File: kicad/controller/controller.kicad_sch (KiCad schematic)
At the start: 39 parts, among them J1 Conn_02x04_Top_Bottom, SW0 1825910-6, SW2 1825910-6, SW3 SW_SPST, SW4 1825910-6, SW6 1825910-6, U1 MCP23S08T-E/SO, U2 MCP3008

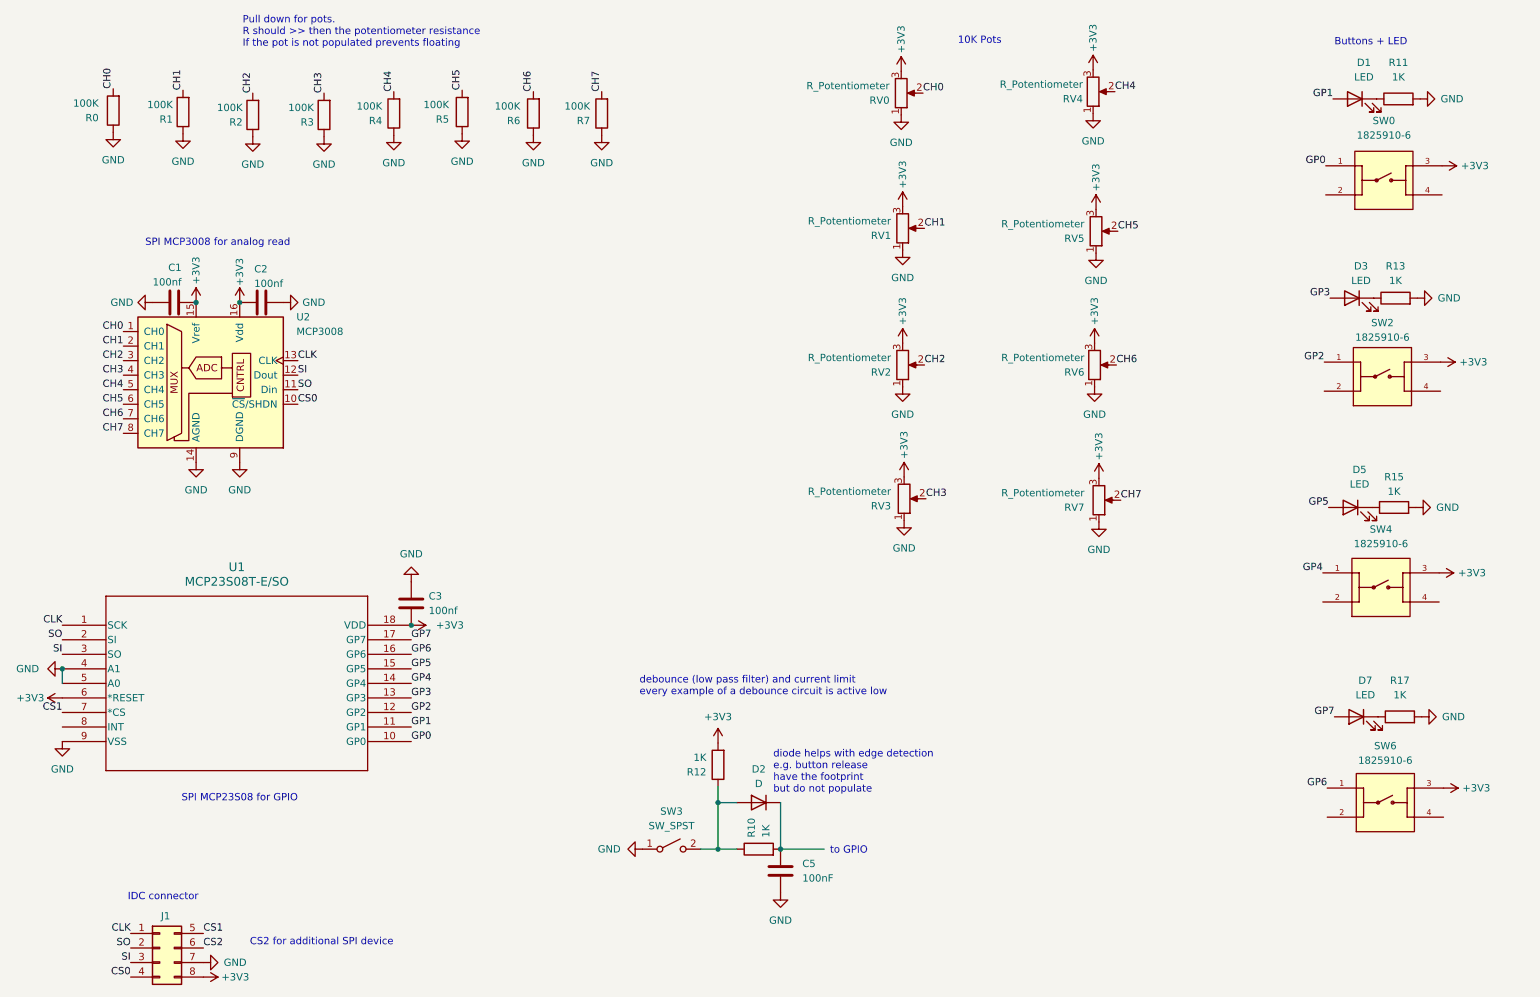
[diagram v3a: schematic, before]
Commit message: fix button behaviour now I have a PCB
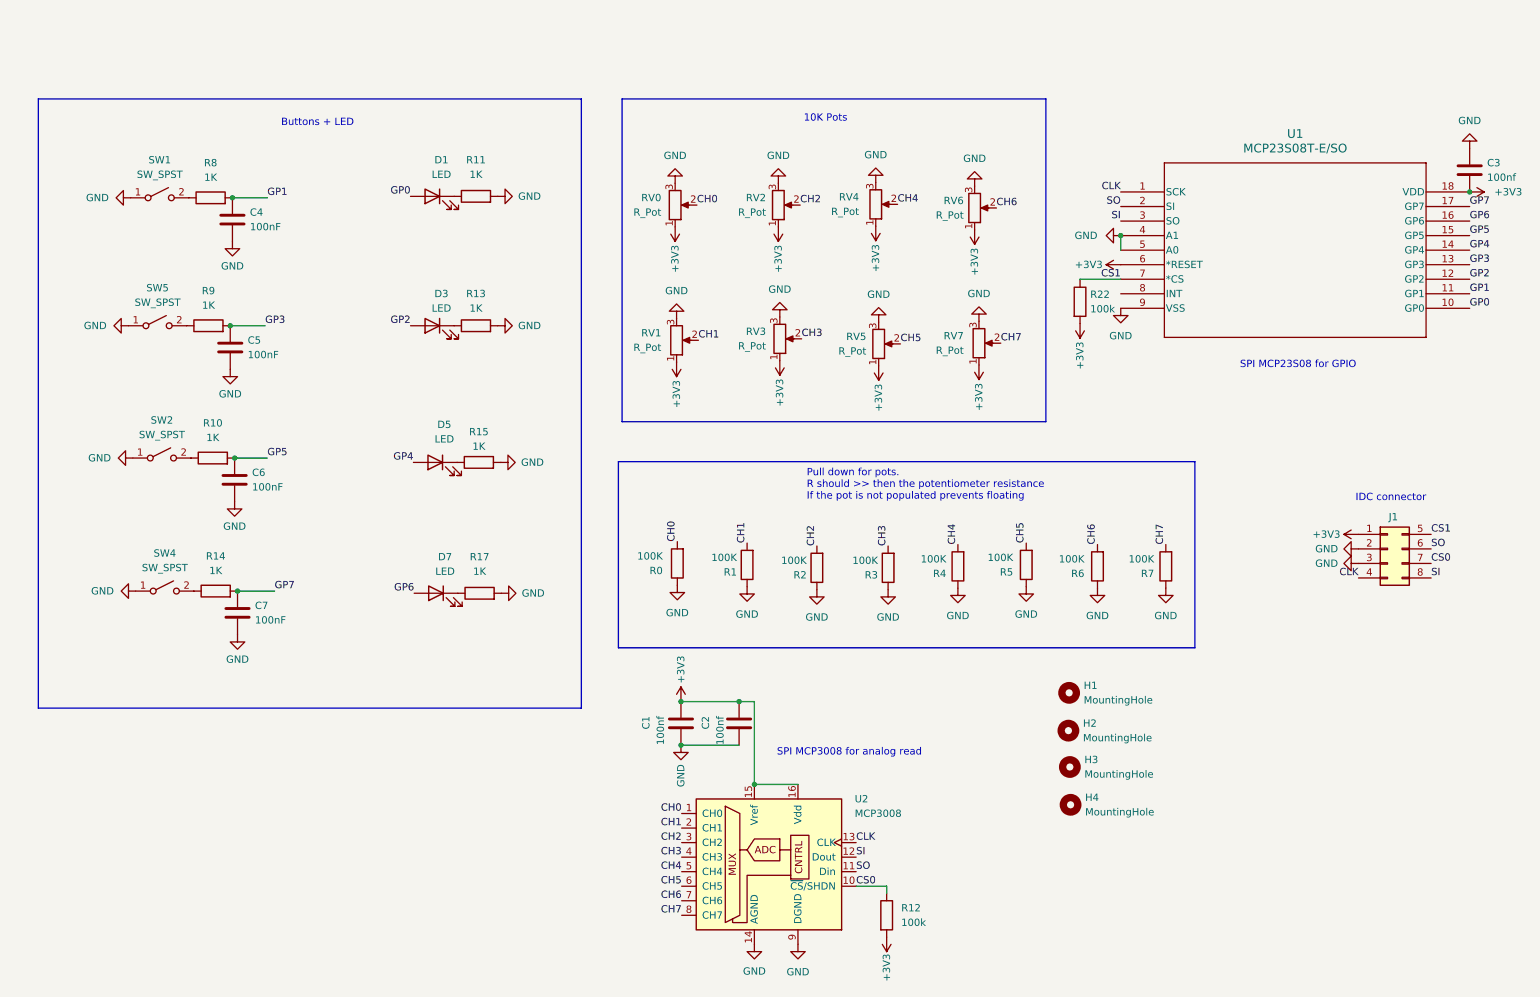
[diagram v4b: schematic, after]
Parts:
- removed D2: D, symbol Device:D
- removed SW0, SW2, SW4, SW6: 1825910-6, Library:SW_1825910-6-4, symbol 2024-07-07_06-52-22:1825910-6
- removed SW3: SW_SPST, symbol Switch:SW_SPST
- added C4, C6, C7: 100nF, symbol Device:C
- added H1, H2, H3, H4: MountingHole, MountingHole:MountingHole_2.7mm_M2.5, symbol Mechanical:MountingHole
- added R14, R8, R9: 1K, symbol Device:R
- added R22: 100k, Resistor_SMD:R_0805_2012Metric, symbol Device:R
- added SW1, SW2, SW4, SW5: SW_SPST, Button_Switch_THT:SW_PUSH-12mm, symbol Switch:SW_SPST
- R12: value 1K -> 100k; footprint (none) -> Resistor_SMD:R_0805_2012Metric
- RV0, RV1, RV2, RV3, RV4, RV5, RV6, RV7: value R_Potentiometer -> R_Pot; footprint Potentiometer_THT:Potentiometer_Alps_RK09K_Single_Vertical -> Potentiometer_THT:Potentiometer_Bourns_PTV09A-1_Single_Vertical
- U1: footprint Library:SOIC18-W_MC_MCH -> Custom:SOIC18-W_MC_MCH
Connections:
- net CS2 is gone; now on net SO: J1.6 (Pin_6)
- net +3V3: now also J1.1 (Pin_1), RV0.1, RV1.1, RV2.1, RV3.1, RV4.1, RV5.1, RV6.1, RV7.1, R22.2; no longer J1.8 (Pin_8), RV0.3, RV1.3, RV2.3, RV3.3, RV4.3, RV5.3, RV6.3, RV7.3
- net CLK: now also J1.4 (Pin_4); no longer J1.1 (Pin_1)
- net CS0: now also J1.7 (Pin_7), R12.1; no longer J1.4 (Pin_4)
- net CS1: now also R22.1
- net GND: now also J1.2 (Pin_2), J1.3 (Pin_3), RV0.3, RV1.3, RV2.3, RV3.3, RV4.3, RV5.3, RV6.3, RV7.3, C4.2, C6.2, C7.2, SW1.1 (A), SW2.1 (A), SW4.1 (A), SW5.1 (A); no longer J1.7 (Pin_7), RV0.1, RV1.1, RV2.1, RV3.1, RV4.1, RV5.1, RV6.1, RV7.1
- net GP0: now also D1.2 (A)
- net GP1: now also C4.1, R8.2; no longer D1.2 (A)
- net GP2: now also D3.2 (A)
- net GP3: now also C5.1, R9.2; no longer D3.2 (A)
- net GP4: now also D5.2 (A)
- net GP5: now also R10.2, C6.1; no longer D5.2 (A)
- net GP6: now also D7.2 (A)
- net GP7: now also C7.1, R14.2; no longer D7.2 (A)
- net SI: now also J1.8 (Pin_8); no longer J1.3 (Pin_3)
- net SO: no longer J1.2 (Pin_2)
- net at R10.1: now also SW2.2 (B); no longer R12.1
- new net: R8.1, SW1.2 (B)
- new net: R9.1, SW5.2 (B)
- new net: R14.1, SW4.2 (B)
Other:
- note removed: "CS2 for additional SPI device"
- note removed: "debounce (low pass filter) and current limit every example of a debounce circuit is active low"
- note removed: "diode helps with edge detection e.g. button release have the footprint but do not populate"
- note removed: "to GPIO"
- moved on the sheet: C1, C2, C3, D1, D3, D5, D7, J1, R0, R1, R11, R13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

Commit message: removed debounce as in practice it did not help
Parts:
- removed C4, C5, C6, C7: 100nF, symbol Device:C
- removed R10, R14, R8, R9: 1K, symbol Device:R
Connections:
- net GP1: now also SW1.2 (B)
- net GP3: now also SW5.2 (B)
- net GP5: now also SW2.2 (B)
- net GP7: now also SW4.2 (B)
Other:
- moved on the sheet: C1, C2, D1, D3, D5, D7, H1, H2, H3, H4, J1, R11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
